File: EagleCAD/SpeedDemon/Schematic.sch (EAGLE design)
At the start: 71 parts, among them Q1 DMC2700, U3 LM3676, U4 STM32F072-LQFP48

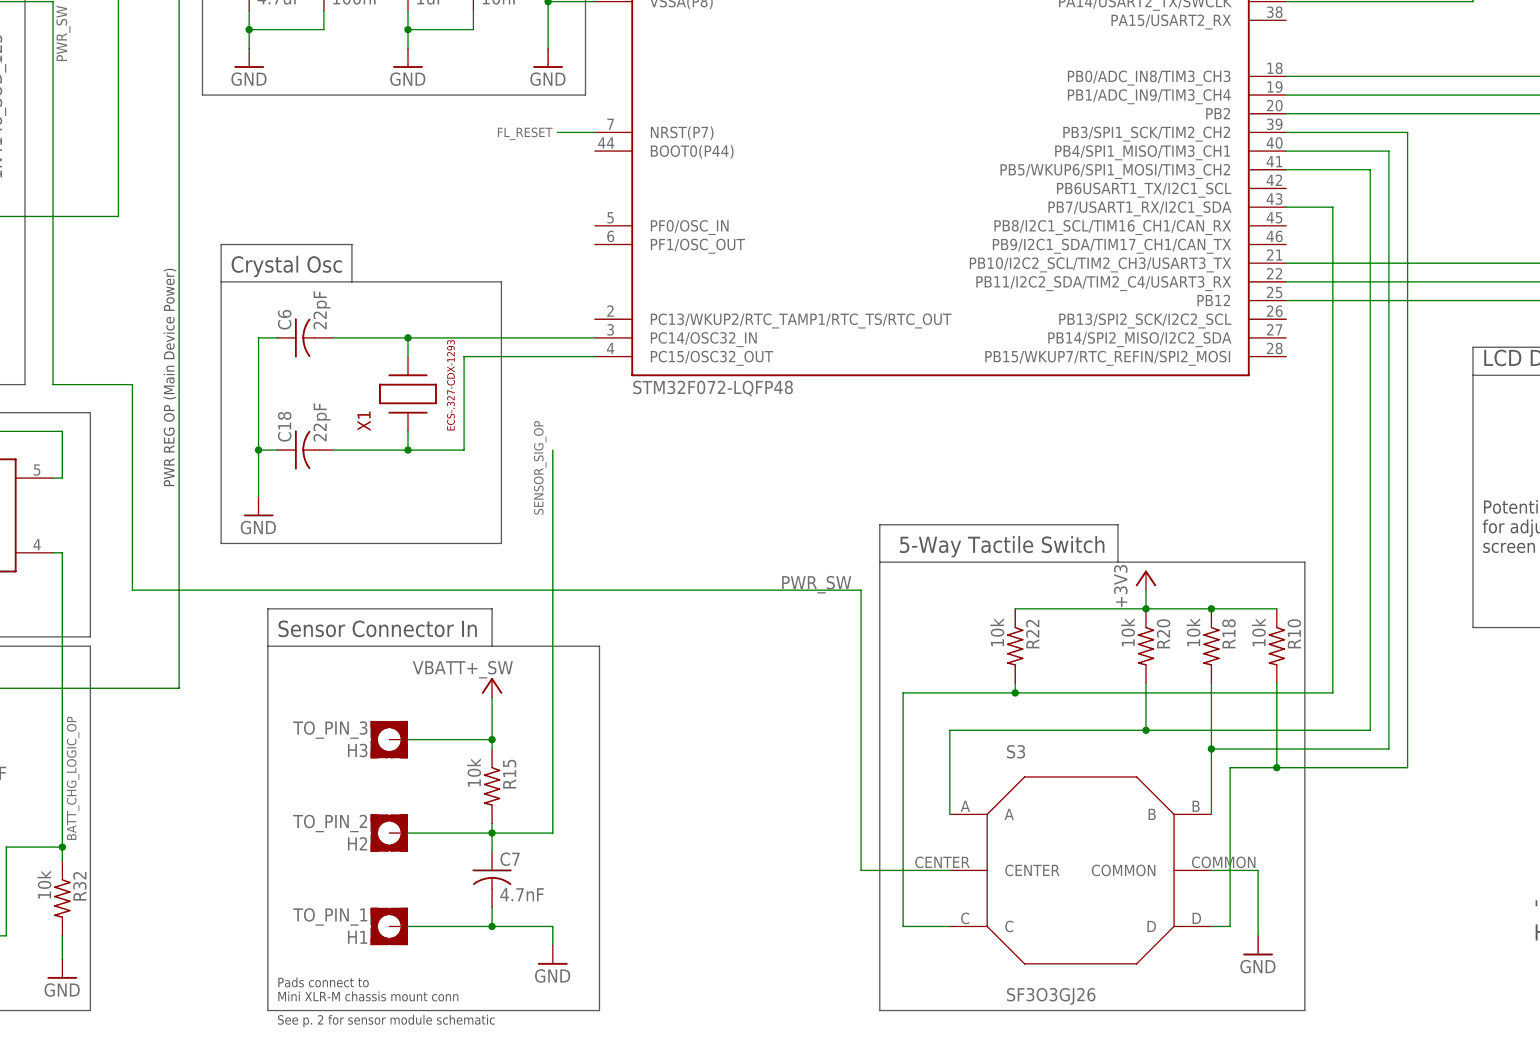
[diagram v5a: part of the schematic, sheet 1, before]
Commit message: Updated the 5-way button
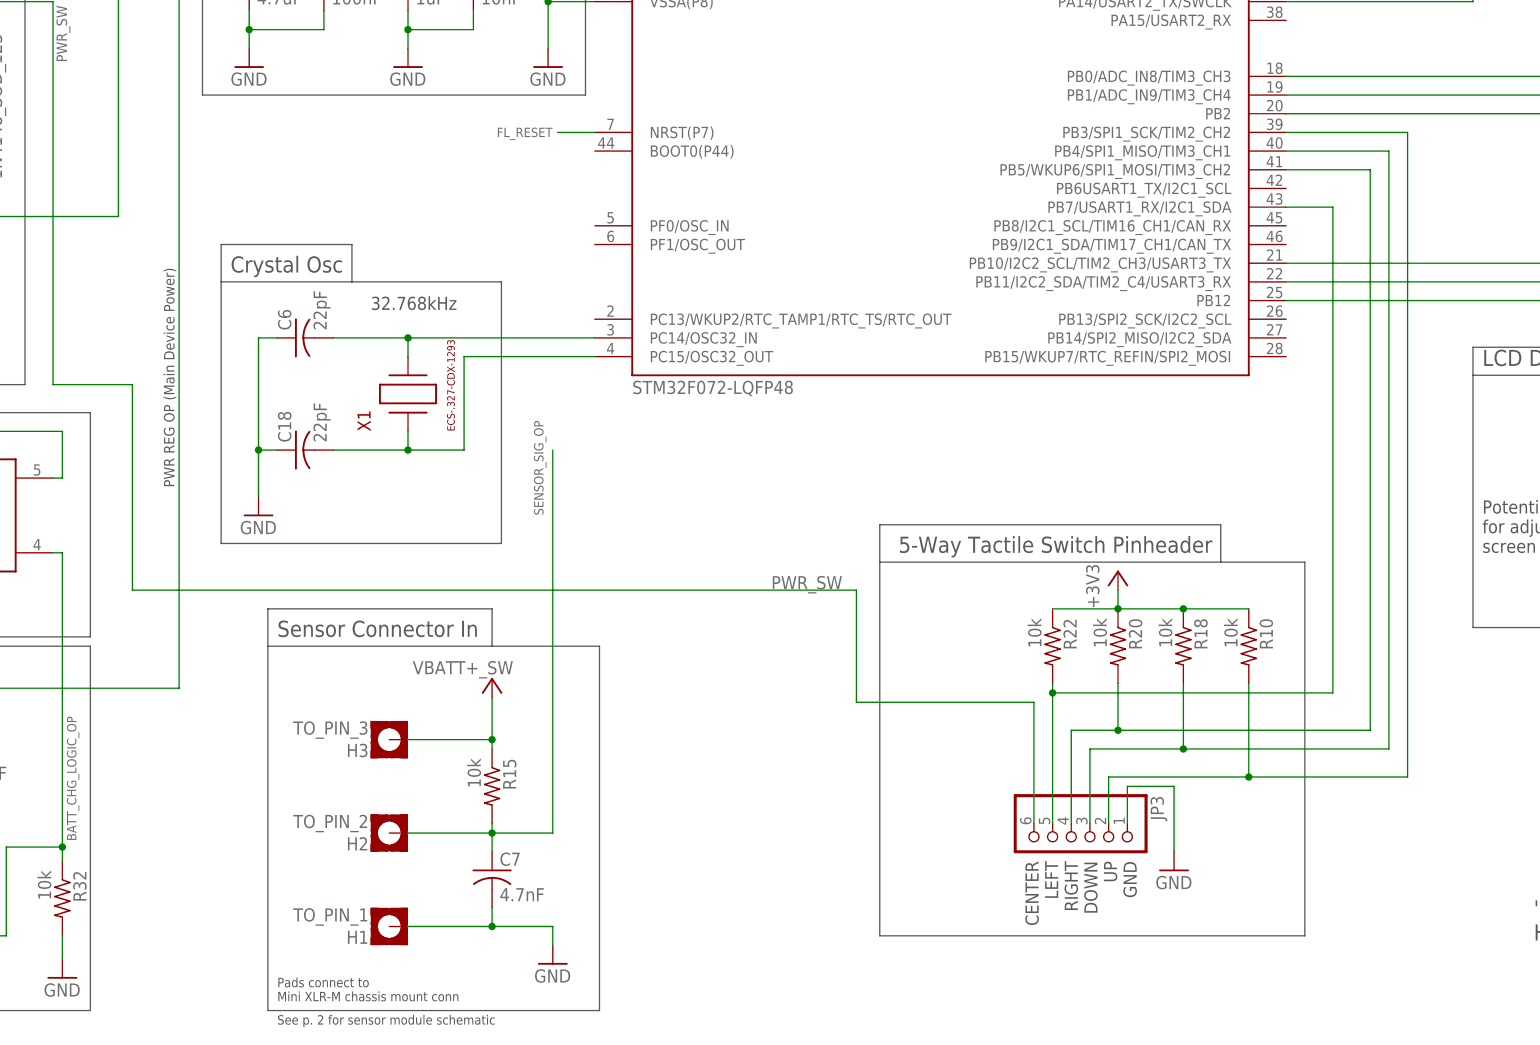
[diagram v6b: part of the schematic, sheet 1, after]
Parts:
- removed S3: SF3O3GJ26, SF3O3GJ26:SF3O3GJ26
- added JP3, JP4: (no value), pinhead:PINHD-1X6
- added S2: (no value), SparkFun-Switches:JOYSTICK_MINI
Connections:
- new net N$26: JP4.6, S2.CENT
- new net N$40: JP4.1, S2.GND
- new net N$41: JP4.4, S2.RIGHT
- new net N$42: JP4.5, S2.LEFT
- new net N$43: JP4.3, S2.DOWN
- new net N$44: JP4.2, S2.UP
- net GND: now also JP3.1; no longer S3.COMMON
- net N$25: now also JP3.5; no longer S3.C
- net N$27: now also JP3.4; no longer S3.A
- net N$29: now also JP3.3; no longer S3.B
- net N$30: now also JP3.2; no longer S3.D
- net PWR_SW: now also JP3.6; no longer S3.CENTER
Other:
- note added: "32.768kHz"
- note added: "5-Way Tactile Switch Breakout Board"
- note added: "5-Way Tactile Switch Pinheader"
- note added: "CENTER LEFT RIGHT DOWN UP GND"
- note removed: "5-Way Tactile Switch"
- moved on the sheet: C17, R10, R18, R20, R22, SIGNAL_OP

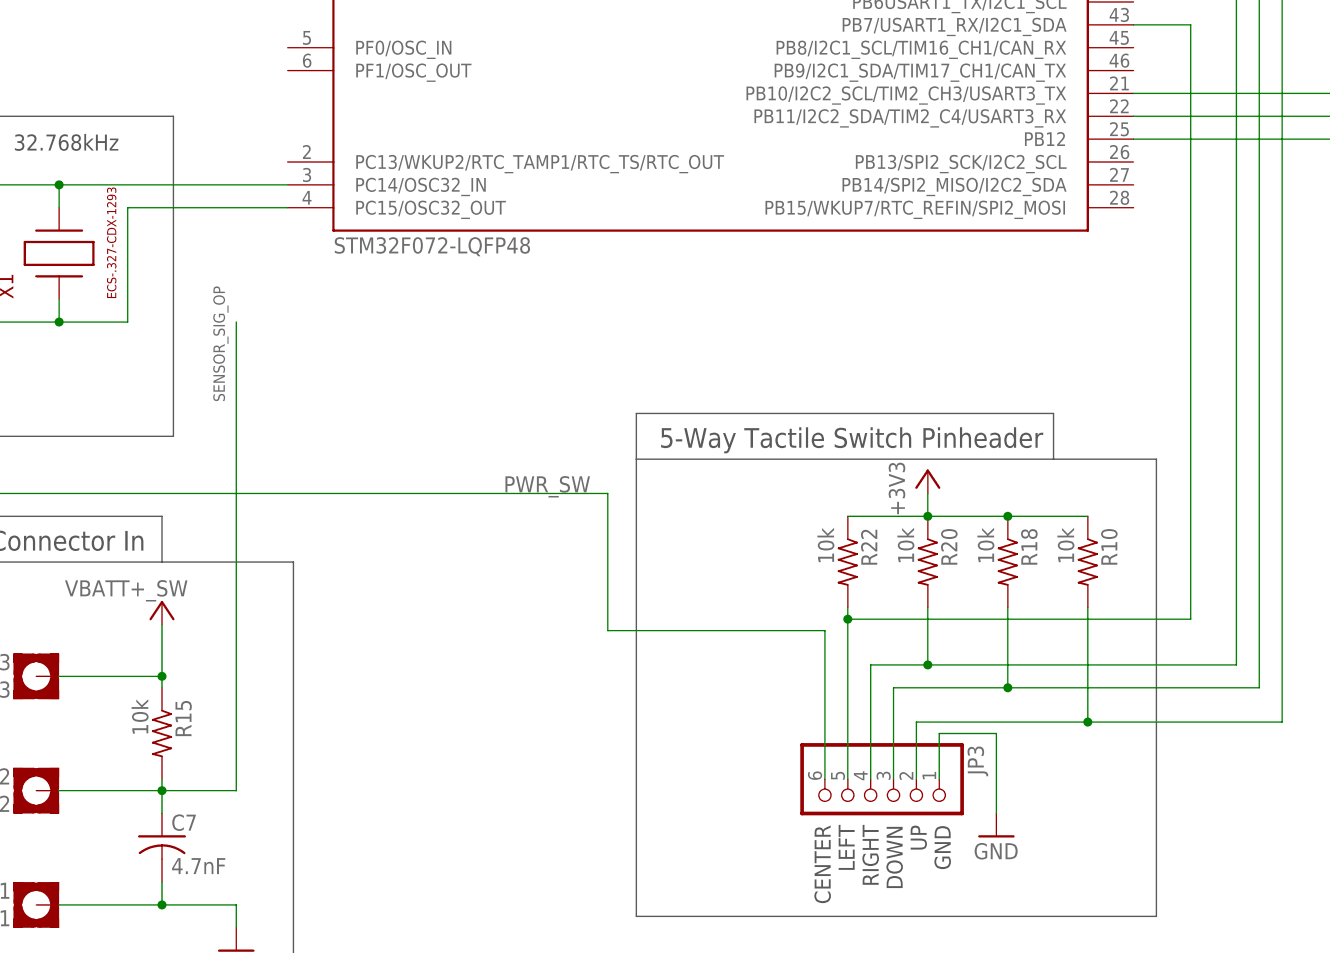
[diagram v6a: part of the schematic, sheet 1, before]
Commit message: Updated 5-way tactile switch
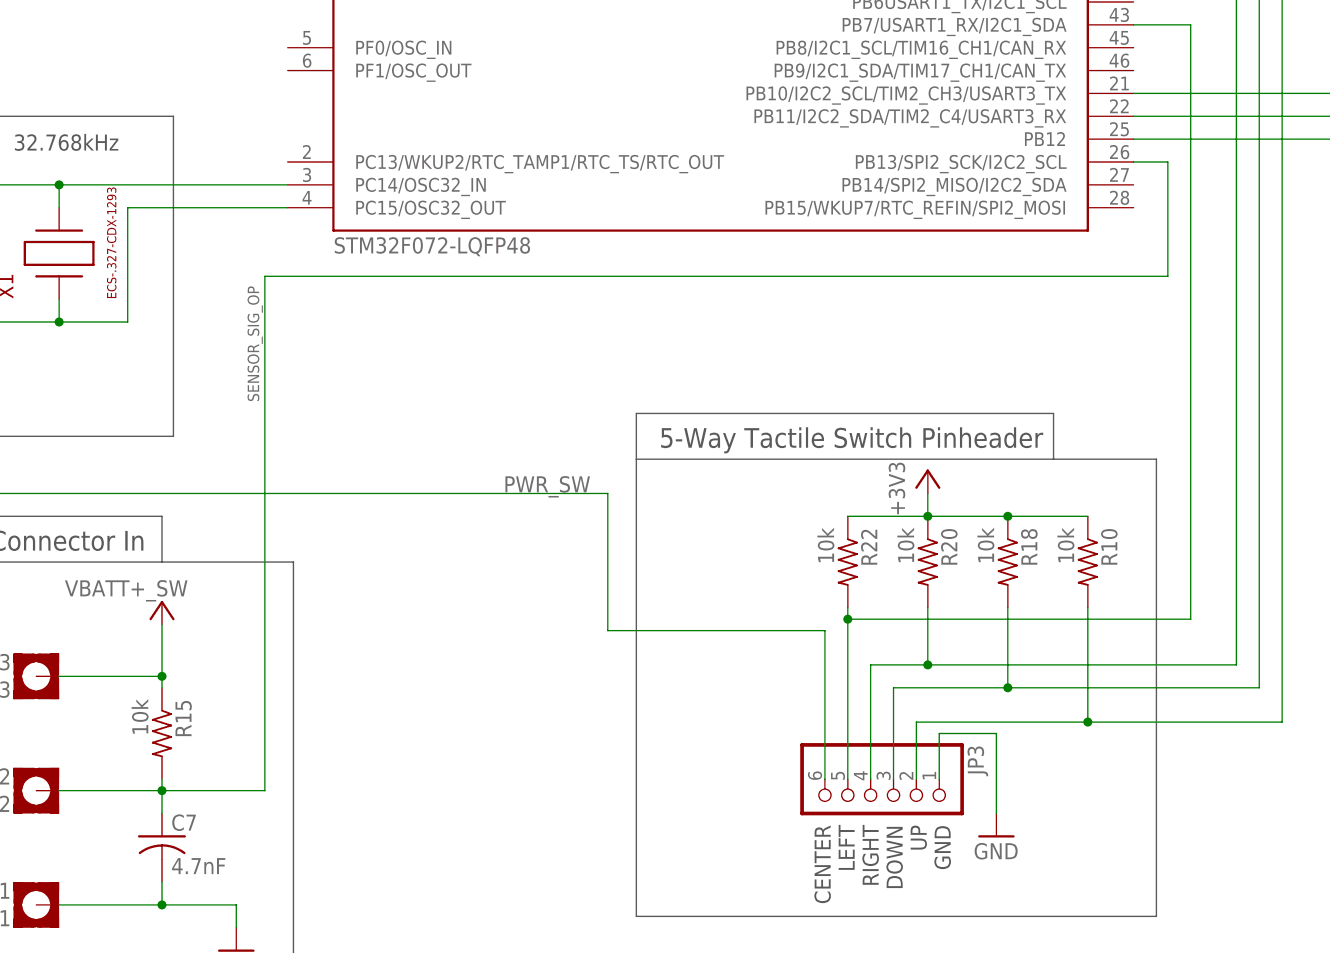
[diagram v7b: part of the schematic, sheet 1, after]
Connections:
- net SENSOR_SIG_OP: now also U4.PB13/SPI2_SCK/I2C2_SCL
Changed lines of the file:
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@@
 <pinref part="C7" gate="G$1" pin="1"/>
 <wire x1="148.59" y1="31.75" x2="148.59" y2="29.21" width="0.1524" layer="91"/>
-<wire x1="148.59" y1="31.75" x2="156.845" y2="31.75" width="0.1524" layer="91"/>
-<label x="155.575" y="74.93" size="1.27" layer="95" rot="R90"/>
-<wire x1="156.845" y1="31.75" x2="156.845" y2="83.82" width="0.1524" layer="91"/>
+<label x="159.385" y="74.93" size="1.27" layer="95" rot="R90"/>
+<wire x1="148.59" y1="31.75" x2="160.02" y2="31.75" width="0.1524" layer="91"/>
+<wire x1="160.02" y1="31.75" x2="160.02" y2="88.9" width="0.1524" layer="91"/>
+<wire x1="160.02" y1="88.9" x2="260.35" y2="88.9" width="0.1524" layer="91"/>
+<pinref part="U4" gate="G$1" pin="PB13/SPI2_SCK/I2C2_SCL"/>
+<wire x1="260.35" y1="88.9" x2="260.35" y2="101.6" width="0.1524" layer="91"/>
+<wire x1="260.35" y1="101.6" x2="256.54" y2="101.6" width="0.1524" layer="91"/>
 </segment>
 </net>

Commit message: Schematic updates, labeling, bus bars. ERC passed. Nathan will finalize tonight.
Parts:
- removed H1: TO_PIN_1, holes:MOUNT-PAD-SQUARE2.8
- removed H2: TO_PIN_2, holes:MOUNT-PAD-SQUARE2.8
- removed H3: TO_PIN_3, holes:MOUNT-PAD-SQUARE2.8
- added JP5: (no value), pinhead:PINHD-1X3
- added R5: 0, rcl:R-US_R0805
- R16: value 1.5M -> 680k
- R17: value 2.2M -> 1M
- X1: value (none) -> 32.768kHz
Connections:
- net N$11 renamed OSC32_OUT
- net N$12 renamed LCD_9_DB2
- net N$13 renamed LCD_10_DB3
- net N$16 renamed LCD_4_RS
- net N$17 renamed LCD_5_R/W
- net N$18 renamed LCD_6_EN
- net N$19 renamed LCD_7_DB0
- net N$20 renamed LCD_8_DB1
- net N$21 renamed LCD_11_DB4
- net N$22 renamed LCD_12_DB5
- net N$23 renamed LCD_13_DB6
- net N$24 renamed LCD_14_DB7
- net N$25 renamed SW_LEFT
- net N$26 renamed SW_CTR_CARD
- net N$27 renamed SW_RIGHT
- net N$29 renamed SW_DOWN
- net N$30 renamed SW_UP
- net N$40 renamed SW_GND_CARD
- net N$41 renamed SW_RIGHT_CARD
- net N$42 renamed SW_LEFT_CARD
- net N$43 renamed SW_DN_CARD
- net N$44 renamed SW_UP_CARD
- new net OSC32_IN: C6.2, R5.1, X1.1
- net GND: now also JP5.1; no longer H1.MOUNT
- net N$5: now also R5.2; no longer C6.2, X1.1
- net SENSOR_SIG_OP: now also JP5.2; no longer H2.MOUNT
- net VBATT+_SW: now also JP5.3; no longer H3.MOUNT
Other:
- note added: "Chip clock runs on x8 freq multiplication"
- note added: "See p.2 for switch connections"
- note added: "Should give ~2.6uA @ ~2.2V. These should work well"
- note added: "Use high drive mode on STM32"
- note added: "Use very low-tolerance capacitors."
- note added: "across all batt voltages (4.3V-3.3V and beyond)."
- note added: "replace with batt pinheader"
- note removed: "32.768kHz"
- note removed: "Aim for ~2.0uA @ min 1.65 max 3.6V. These should work well"
- note removed: "May have to change resistor vals depending on battery used."
- note removed: "with max 6.1V from the battery across all charge ranges."
- moved on the sheet: C17, C18, C6, C7, JP4, R15, S2, SIGNAL_OP
